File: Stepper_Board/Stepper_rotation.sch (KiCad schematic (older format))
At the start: 14 parts

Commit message: Testsoftware for ImageProcessing in c programmiert
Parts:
- removed C?: 2.2u 16V, Capacitor_SMD:C_0603_1608Metric, symbol Device:C_Small
- removed C?: 22n 50V, Capacitor_SMD:C_0603_1608Metric, symbol Device:C_Small
- removed C? (x2): 100n 50V, Capacitor_SMD:C_0603_1608Metric, symbol Device:C_Small
- removed C?: 100u 35V, Capacitor_THT:CP_Radial_D6.3mm_P2.50mm, symbol Device:CP_Small
- removed C?: 1u 16V, Capacitor_SMD:C_0603_1608Metric, symbol Device:C_Small
- removed R? (x2): 0.1R 0.5W, Resistor_SMD:R_1210_3225Metric, symbol Device:R_Small
- removed R?: 22k, Resistor_SMD:R_0603_1608Metric, symbol Device:R_Small
- removed SW?: SW_DIP_x03, Package_DIP:DIP-6_W7.62mm, symbol Switch:SW_DIP_x03
- removed U?: TMC2226, Package_SO:TSSOP-28-1EP_4.4x9.7mm_P0.65mm, symbol Pick_n_Place:TMC2226
- added C501, C507: 100n 50V, Capacitor_SMD:C_0603_1608Metric, symbol Device:C_Small
- added C502: 2.2u 16V, Capacitor_SMD:C_0603_1608Metric, symbol Device:C_Small
- added C503: 1u 16V, Capacitor_SMD:C_0603_1608Metric, symbol Device:C_Small
- added C504: 22n 50V, Capacitor_SMD:C_0603_1608Metric, symbol Device:C_Small
- added C509: 100u 35V, Capacitor_THT:CP_Radial_D6.3mm_P2.50mm, symbol Device:CP_Small
- added R501: 22k, Resistor_SMD:R_0603_1608Metric, symbol Device:R_Small
- added R502, R503: 0.1R 0.5W, Resistor_SMD:R_1210_3225Metric, symbol Device:R_Small
- added SW501: SW_DIP_x03, Package_DIP:DIP-6_W7.62mm, symbol Switch:SW_DIP_x03
- added U501: TMC2226-Pick_n_Place, Package_SO:TSSOP-28-1EP_4.4x9.7mm_P0.65mm, symbol StepperBoard-rescue:TMC2226-Pick_n_Place
- gave numbers to parts that had none: 3

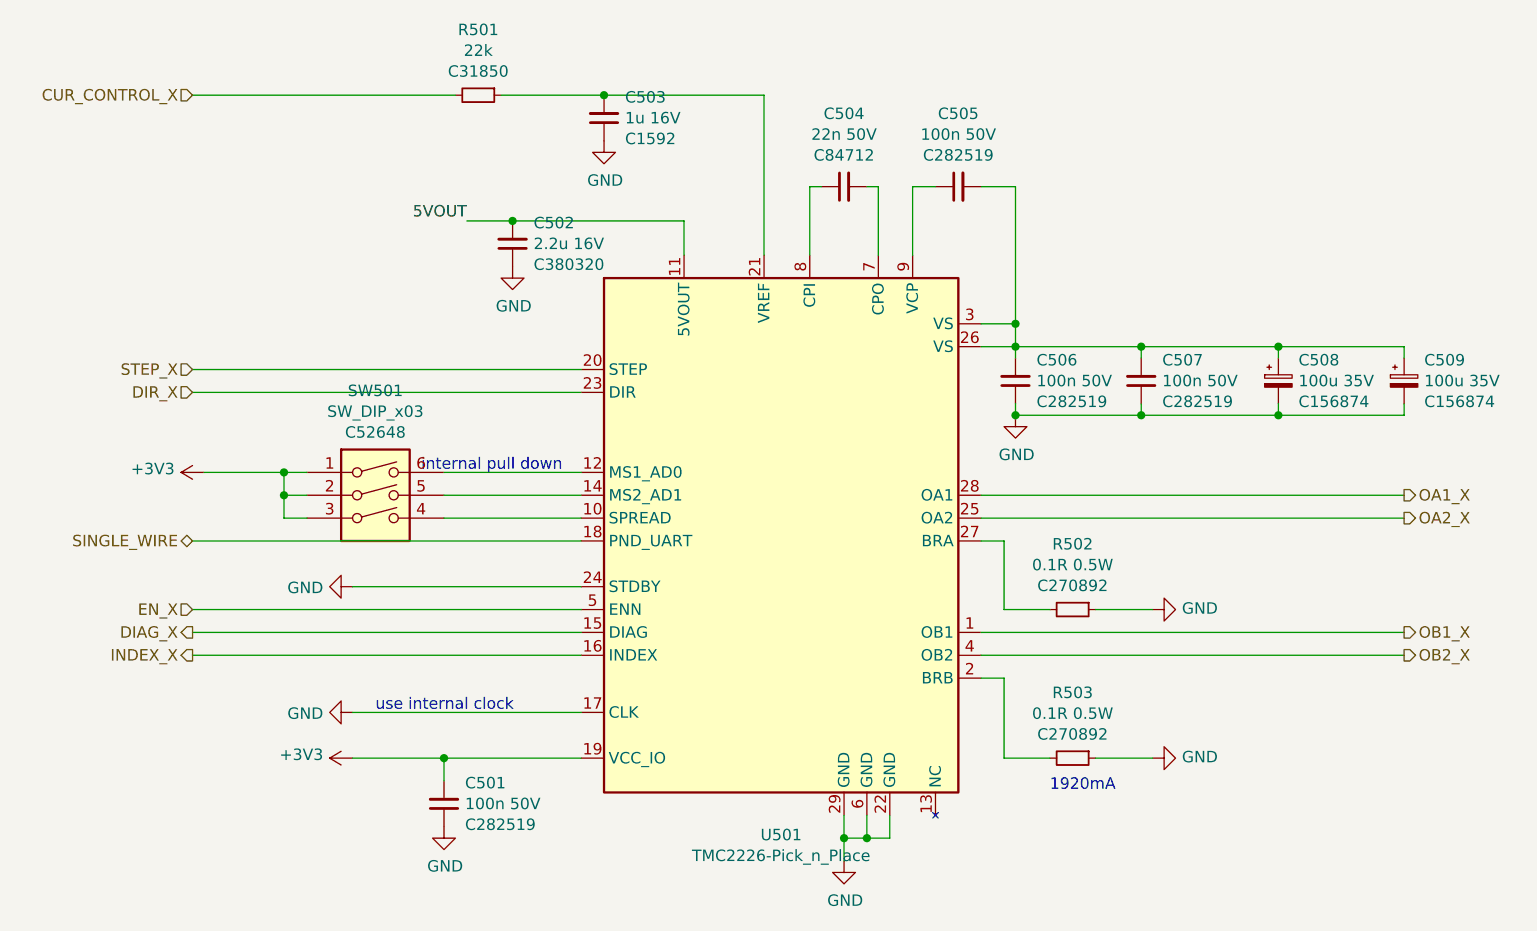
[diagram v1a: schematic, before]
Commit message: STM32F401 für motoransteuerung gewählt. TODO: motoransteuerung und leistungsteil trennen, damit für schnelle fehlerbehebung modul getauscht werden kann
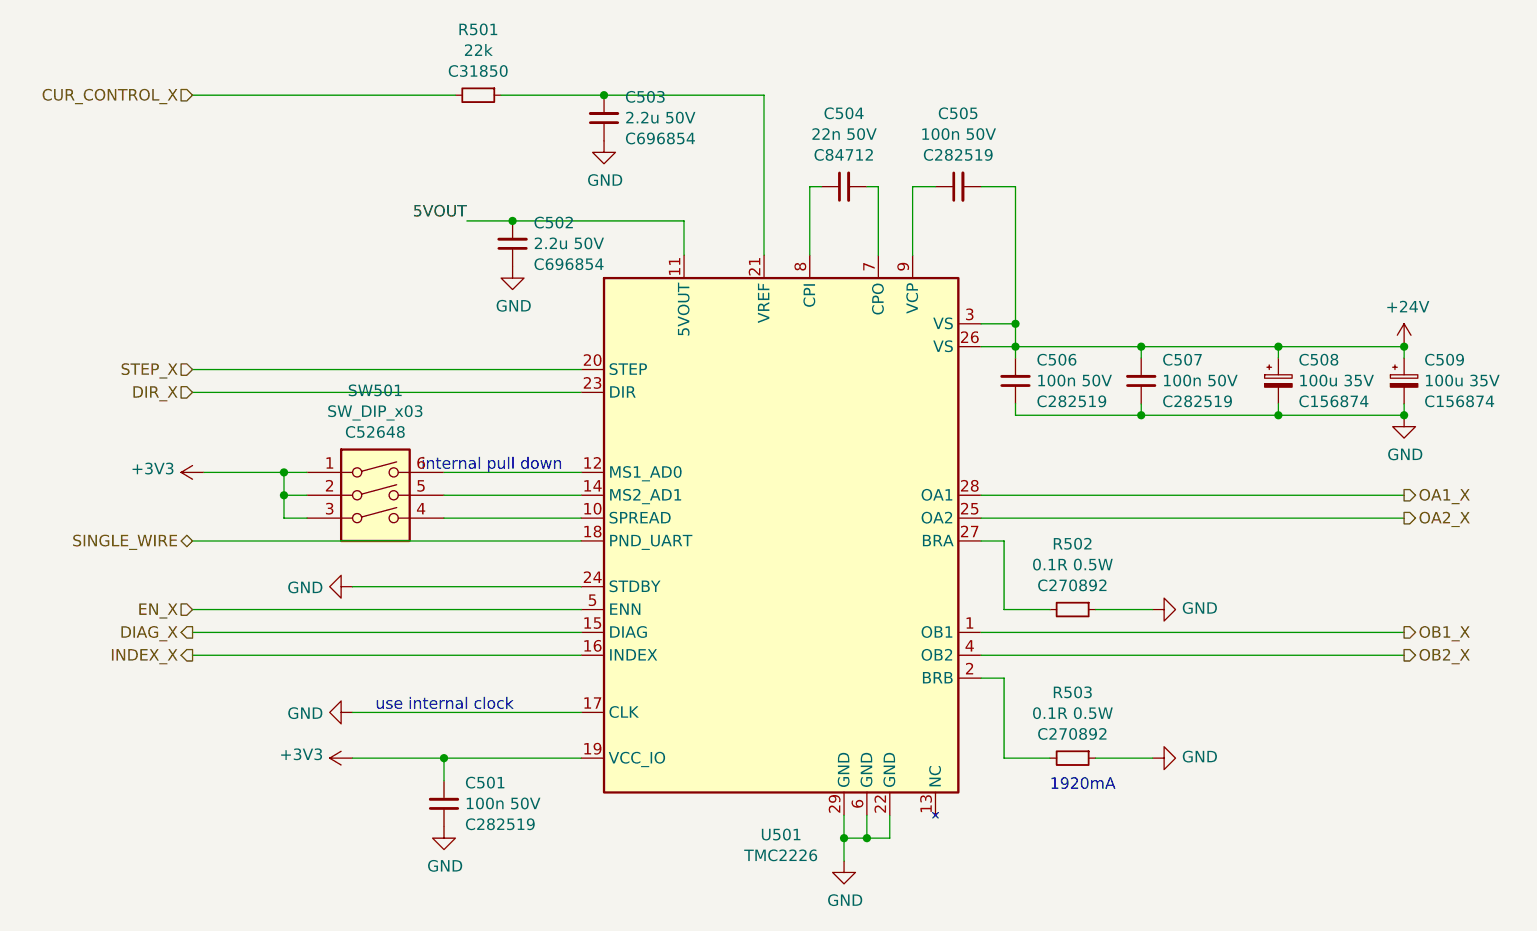
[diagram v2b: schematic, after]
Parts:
- C502: value 2.2u 16V -> 2.2u 50V; footprint Capacitor_SMD:C_0603_1608Metric -> Capacitor_SMD:C_1210_3225Metric; LCSC C380320 -> C696854
- C503: value 1u 16V -> 2.2u 50V; footprint Capacitor_SMD:C_0603_1608Metric -> Capacitor_SMD:C_1210_3225Metric; LCSC C1592 -> C696854
- U501: value TMC2226-Pick_n_Place -> TMC2226; LCSC (none) -> C705366
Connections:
- net +24V: now reaches C505.2, C506.2, C507.2, C508.1, C509.1, U501.26 (VS), U501.3 (VS)
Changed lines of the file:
@@
 AR Path="/5FCB2242/5FCB6218" Ref="C502"  Part="1"
 F 0 "C502" H 5458 1509 50  0000 R CNN
-F 1 "2.2u 16V" H 5458 1600 50  0000 R CNN
-F 2 "Capacitor_SMD:C_0603_1608Metric" H 5550 1600 50  0001 C CNN
+F 1 "2.2u 50V" H 5458 1600 50  0000 R CNN
+F 2 "Capacitor_SMD:C_1210_3225Metric" H 5550 1600 50  0001 C CNN
 F 3 "~" H 5550 1600 50  0001 C CNN
-F 4 "C380320 " H 5458 1691 50  0000 R CNN "LCSC"
+F 4 " C696854 " H 5458 1691 50  0000 R CNN "LCSC"
 	1    5550 1600
 	-1   0    0    1
@@
 L power:GND #PWR?
 U 1 1 5FBD5713
-P 7750 2350
+P 9450 2350
 AR Path="/5FBD329F/5FBD5713" Ref="#PWR?"  Part="1"
 AR Path="/5FBFC277/5FBD5713" Ref="#PWR?"  Part="1"
@@
 AR Path="/5FBFCAC4/5FBD5713" Ref="#PWR0136"  Part="1"
 AR Path="/5FCB2242/5FBD5713" Ref="#PWR0138"  Part="1"
-F 0 "#PWR0138" H 7750 2100 50  0001 C CNN
-F 1 "GND" H 7755 2177 50  0000 C CNN
-F 2 "" H 7750 2350 50  0001 C CNN
-F 3 "" H 7750 2350 50  0001 C CNN
-	1    7750 2350
+F 0 "#PWR0138" H 9450 2100 50  0001 C CNN
+F 1 "GND" H 9455 2177 50  0000 C CNN
+F 2 "" H 9450 2350 50  0001 C CNN
+F 3 "" H 9450 2350 50  0001 C CNN
+	1    9450 2350
 	1    0    0    -1
 $EndComp
@@
 Wire Wire Line
 	7750 2300 7750 2350
-Connection ~ 7750 2350
 $Comp
 L Device:CP_Small C?
@@
 AR Path="/5FCB2242/5FCB6245" Ref="C503"  Part="1"
 F 0 "C503" H 5858 959 50  0000 R CNN
-F 1 "1u 16V" H 5858 1050 50  0000 R CNN
-F 2 "Capacitor_SMD:C_0603_1608Metric" H 5950 1050 50  0001 C CNN
+F 1 "2.2u 50V" H 5858 1050 50  0000 R CNN
+F 2 "Capacitor_SMD:C_1210_3225Metric" H 5950 1050 50  0001 C CNN
 F 3 "~" H 5950 1050 50  0001 C CNN
-F 4 "C1592" H 5858 1141 50  0000 R CNN "LCSC"
+F 4 " C696854 " H 5858 1141 50  0000 R CNN "LCSC"
 	1    5950 1050
 	-1   0    0    1
@@
 P 6450 2650
 F 0 "U501" H 6725 1114 50  0000 C CNN
-F 1 "TMC2226-Pick_n_Place" H 6725 1023 50  0000 C CNN
+F 1 "TMC2226" H 6725 1023 50  0000 C CNN
 F 2 "Package_SO:TSSOP-28-1EP_4.4x9.7mm_P0.65mm" H 6700 850 50  0001 C CNN
-F 3 "" H 5300 3700 50  0001 C CNN
+F 3 "https://datasheet.lcsc.com/szlcsc/2007202037_TRINAMIC-Motion-Control-GmbH-TMC2226-SA-T_C705366.pdf" H 5300 3700 50  0001 C CNN
+F 4 "C705366" H 6450 2650 50  0001 C CNN "LCSC"
 	1    6450 2650
 	1    0    0    -1
 $EndComp
+$Comp
+L power:+24V #PWR0501
+U 1 1 6004CACE
+P 9450 2050
+F 0 "#PWR0501" H 9450 1900 50  0001 C CNN
+F 1 "+24V" H 9465 2223 50  0000 C CNN
+F 2 "" H 9450 2050 50  0001 C CNN
+F 3 "" H 9450 2050 50  0001 C CNN
+	1    9450 2050
+	1    0    0    -1
+$EndComp
+Connection ~ 9450 2050
+Connection ~ 9450 2350
 $EndSCHEMATC
